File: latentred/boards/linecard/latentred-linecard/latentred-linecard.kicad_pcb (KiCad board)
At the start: 4 copper layers, 220 x 92 mm, 439 parts, among them J1 CONN_LATENTRED_LINECARD_DEVICE, J2 STEWART_SS_74500_024, Q1 SSM6N58NU, Q2 SSM6N58NU, Q3 SSM6N58NU, Q4 SSM6N58NU, Q5 SSM6N58NU, Q6 SSM6N58NU, Q7 SSM6N58NU, Q8 SSM6N58NU, U1 MCP1703T-3302E, U10 DP83867, U11 DP83867, U12 DP83867, U13 DP83867, U14 DP83867, U15 DP83867, U16 DSC6101CI2A-025.0000, U17 5PB1108CMG, U2 LTC3374-QFN, U3 SI7050, U4 LTC2451, U5 INA226, U6 INA226, U7 INA226, U8 DP83867, U9 DP83867

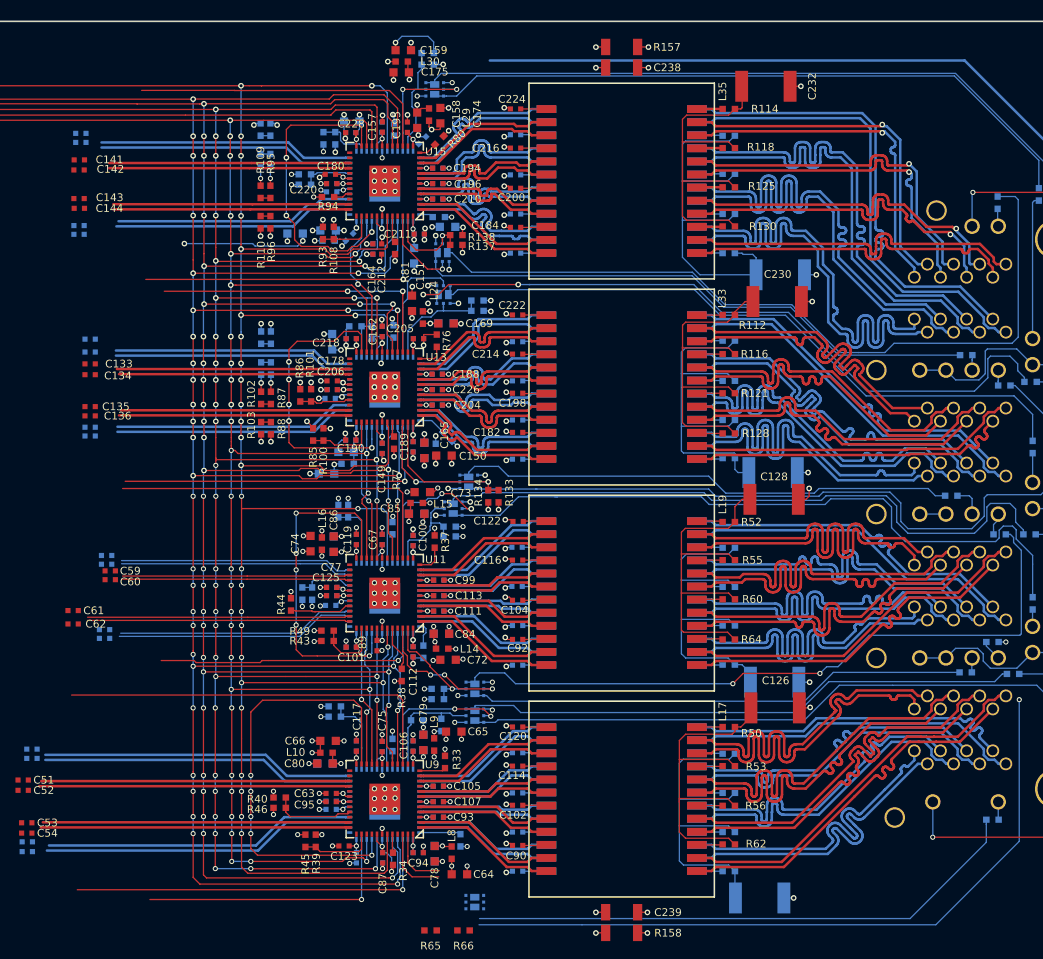
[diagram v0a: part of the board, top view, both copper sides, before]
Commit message: Removed meanders from MDI traces as per Intel layout manual. Now only doing skew matching.
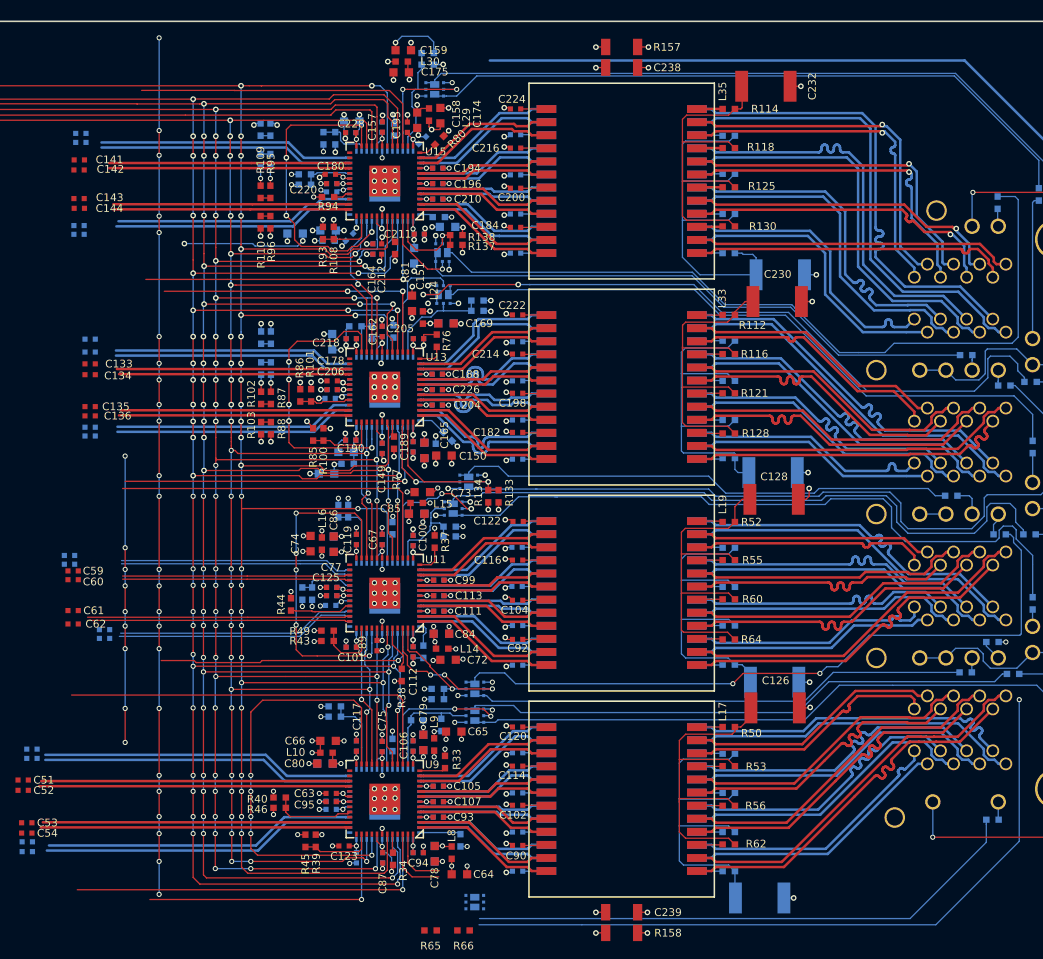
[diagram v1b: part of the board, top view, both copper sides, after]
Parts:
- moved C57 3.60 mm to (170.4, 66.2)
- moved C58 3.60 mm to (170.4, 65.3)
- moved C59 3.60 mm to (170.8, 66.8)
- moved C60 3.60 mm to (170.8, 67.7)
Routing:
- net /PHYs/2V5: track 189.6 -> 255.2 mm, vias 5 -> 29
- net /PHYs/1V0: track 130.2 -> 155.9 mm, vias 8 -> 17
- net /PHYs/ETH6_DM_N: track 46.5 -> 28.8 mm
- net /PHYs/ETH6_DM_P: track 46.5 -> 28.8 mm
- net /PHYs/ETH4_DM_N: track 36.6 -> 23.9 mm
- net /PHYs/ETH4_DM_P: track 36.6 -> 23.9 mm
- net /PHYs/ETH1_DM_N: track 37.1 -> 24.9 mm
- net /PHYs/ETH1_DM_P: track 37.1 -> 24.9 mm
- net /PHYs/ETH6_CM_N: track 46.5 -> 34.5 mm
- net /PHYs/ETH6_CM_P: track 46.5 -> 34.5 mm
- net /PHYs/ETH3_DM_N: track 34.6 -> 23.1 mm
- net /PHYs/ETH3_DM_P: track 34.6 -> 23.1 mm
- net /PHYs/ETH2_DM_P: track 34.1 -> 23.7 mm
- net /PHYs/ETH2_DM_N: track 34.1 -> 23.7 mm
- net /PHYs/ETH4_CM_N: track 36.6 -> 28.4 mm
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
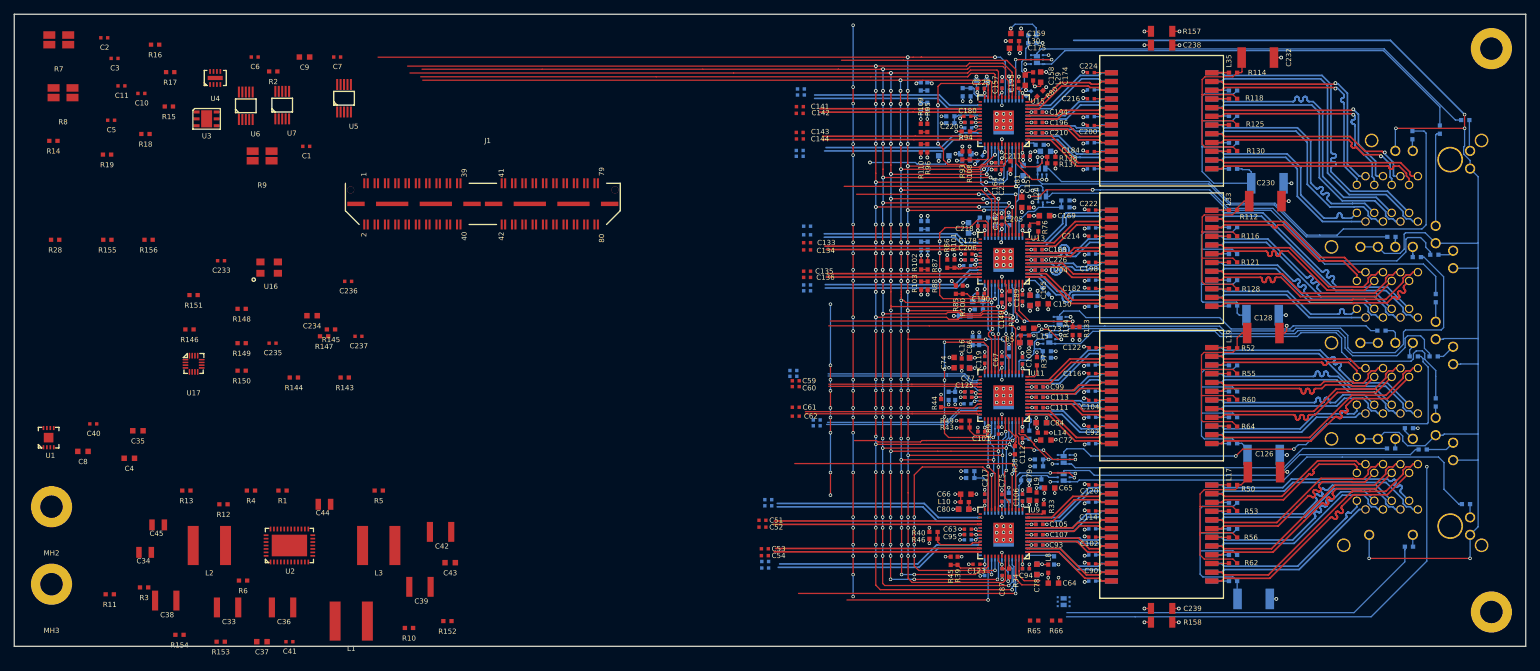
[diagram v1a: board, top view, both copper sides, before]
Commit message: Continued initial line card layout
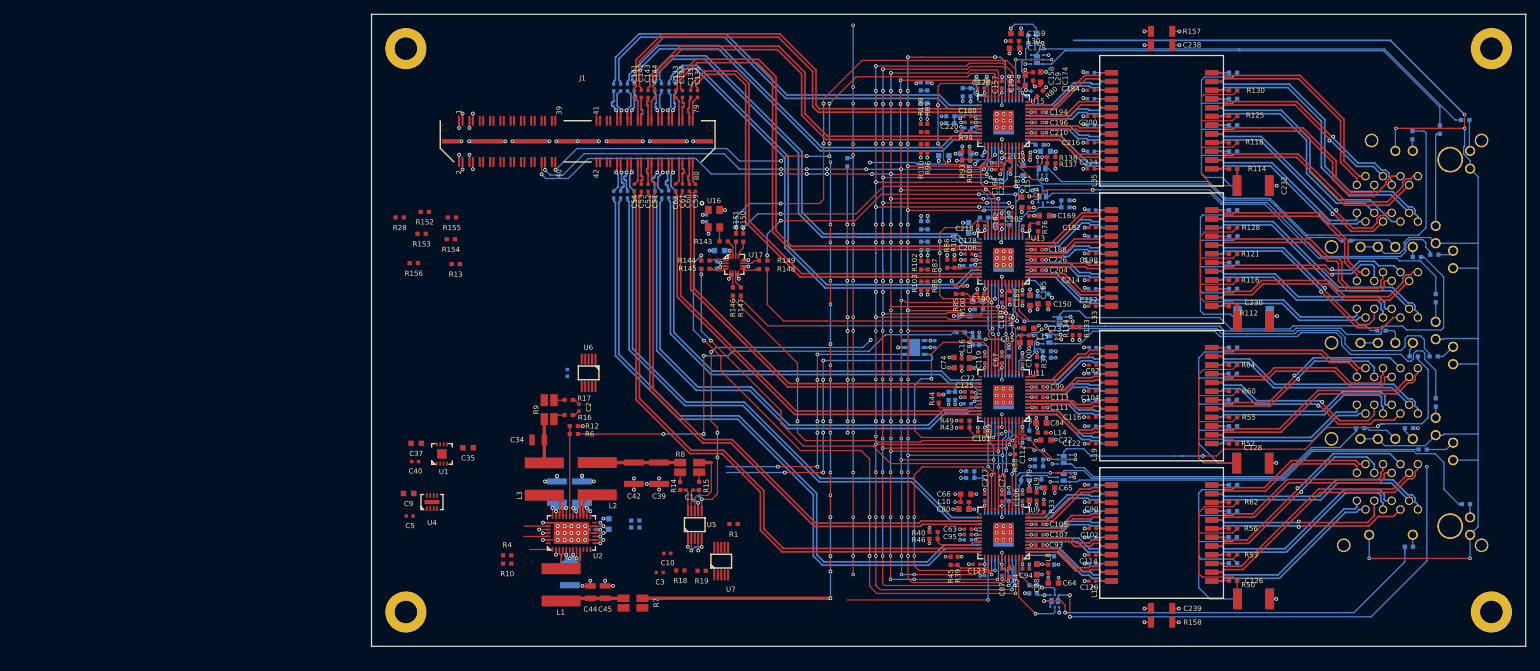
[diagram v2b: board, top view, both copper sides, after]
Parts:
- removed C4, C8: 4.7 uF, azonenberg_pcb:EIA_0603_CAP_NOSILK
- C11, C233, C234, C235, C236, C237, C33, C36, C38, C41, C43, C6, C7, R11, R2, R3, R5, R65, R66, U3: moved to B.Cu
- moved R3 124.5 mm to (194.8, 59.8)
- moved R7 117.1 mm to (147.1, 99.2), turned to 180 degrees
- moved C3 109.1 mm to (150.9, 94.8)
- moved U3 108.3 mm to (188.1, 62.0)
- moved C6 107.5 mm to (191.0, 61.5), turned to 90 degrees
- moved R8 106.3 mm to (155.3, 79.5), turned to 180 degrees
- moved R19 105.6 mm to (157.1, 94.5)
- moved R14 104.1 mm to (153.9, 82.2), turned to 270 degrees
- moved C10 101.7 mm to (152.1, 92.0)
- moved R18 100.5 mm to (153.9, 94.5)
- moved R15 94.9 mm to (156.7, 82.2), turned to 270 degrees
- moved U7 92.1 mm to (159.9, 93.1)
- moved C2 87.6 mm to (139.2, 70.8), turned to 90 degrees
- moved R2 84.6 mm to (178.2, 35.0), turned to 90 degrees
- moved MH2 84.3 mm to (114.0, 18.5), turned to 45 degrees
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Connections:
- J1 pad 18: /JTAG_TDI -> (no net)
- J1 pad 20: /JTAG_TDO -> (no net)
- J1 pad 22: /JTAG_TMS -> (no net)
- J1 pad 24: /JTAG_TCK -> (no net)
- J1 pad 34: (no net) -> /JTAG_TCK
- J1 pad 36: (no net) -> /JTAG_TMS
- J1 pad 38: (no net) -> /JTAG_TDI
- J1 pad 40: /PHYs/SGMII0_TX_P -> /JTAG_TDO
- J1 pad 41: /SGMII0_RX_P -> (no net)
- J1 pad 42: /PHYs/SGMII0_TX_N -> (no net)
- J1 pad 43: /SGMII0_RX_N -> (no net)
- J1 pad 44: /PHYs/SGMII1_TX_P -> (no net)
- J1 pad 45: /SGMII1_RX_P -> (no net)
- J1 pad 46: /PHYs/SGMII1_TX_N -> (no net)
- J1 pad 47: /SGMII1_RX_N -> (no net)
- J1 pad 48: /PHYs/SGMII2_TX_P -> (no net)
- J1 pad 49: /SGMII2_RX_P -> /SGMII6_RX_N
- J1 pad 50: /PHYs/SGMII2_TX_N -> /PHYs/SGMII0_TX_P
- J1 pad 51: /SGMII2_RX_N -> /SGMII6_RX_P
- J1 pad 52: /PHYs/SGMII3_TX_P -> /PHYs/SGMII0_TX_N
- J1 pad 53: /SGMII3_RX_P -> /PHYs/SGMII6_TX_N
- J1 pad 54: /PHYs/SGMII3_TX_N -> /SGMII0_RX_P
- J1 pad 55: /SGMII3_RX_N -> /PHYs/SGMII6_TX_P
- J1 pad 56: /PHYs/SGMII4_TX_P -> /SGMII0_RX_N
- J1 pad 57: /SGMII4_RX_P -> /PHYs/SGMII7_TX_P
- J1 pad 58: /PHYs/SGMII4_TX_N -> /SGMII1_RX_N
- J1 pad 59: /SGMII4_RX_N -> /PHYs/SGMII7_TX_N
- J1 pad 60: /PHYs/SGMII5_TX_P -> /SGMII1_RX_P
- J1 pad 61: /SGMII5_RX_P -> /SGMII7_RX_P
- J1 pad 62: /PHYs/SGMII5_TX_N -> /PHYs/SGMII1_TX_N
- J1 pad 63: /SGMII5_RX_N -> /SGMII7_RX_N
- J1 pad 64: /PHYs/SGMII6_TX_P -> /PHYs/SGMII1_TX_P
- J1 pad 65: /SGMII6_RX_P -> /SGMII4_RX_N
- J1 pad 66: /PHYs/SGMII6_TX_N -> /PHYs/SGMII2_TX_P
- J1 pad 67: /SGMII6_RX_N -> /SGMII4_RX_P
- J1 pad 68: /PHYs/SGMII7_TX_P -> /PHYs/SGMII2_TX_N
- J1 pad 69: /SGMII7_RX_P -> /PHYs/SGMII4_TX_N
- J1 pad 70: /PHYs/SGMII7_TX_N -> /SGMII2_RX_P
- J1 pad 71: /SGMII7_RX_N -> /PHYs/SGMII4_TX_P
- J1 pad 72: (no net) -> /SGMII2_RX_N
- J1 pad 73: (no net) -> /PHYs/SGMII5_TX_P
- J1 pad 74: (no net) -> /SGMII3_RX_N
- J1 pad 75: (no net) -> /PHYs/SGMII5_TX_N
- J1 pad 76: (no net) -> /SGMII3_RX_P
- J1 pad 77: (no net) -> /SGMII5_RX_P
- J1 pad 78: (no net) -> /PHYs/SGMII3_TX_N
- J1 pad 79: (no net) -> /SGMII5_RX_N
- J1 pad 80: (no net) -> /PHYs/SGMII3_TX_P
- J2 pad A4: /PHYs/ETH0_BM_N -> /PHYs/ETH0_CM_P
- J2 pad A5: /PHYs/ETH0_CM_P -> /PHYs/ETH0_CM_N
- J2 pad A6: /PHYs/ETH0_CM_N -> /PHYs/ETH0_BM_N
- J2 pad B4: /PHYs/ETH1_BM_N -> /PHYs/ETH1_CM_P
- J2 pad B5: /PHYs/ETH1_CM_P -> /PHYs/ETH1_CM_N
- J2 pad B6: /PHYs/ETH1_CM_N -> /PHYs/ETH1_BM_N
- J2 pad C4: /PHYs/ETH2_BM_N -> /PHYs/ETH2_CM_P
- J2 pad C5: /PHYs/ETH2_CM_P -> /PHYs/ETH2_CM_N
- J2 pad C6: /PHYs/ETH2_CM_N -> /PHYs/ETH2_BM_N
- J2 pad D4: /PHYs/ETH3_BM_N -> /PHYs/ETH3_CM_P
- J2 pad D5: /PHYs/ETH3_CM_P -> /PHYs/ETH3_CM_N
- J2 pad D6: /PHYs/ETH3_CM_N -> /PHYs/ETH3_BM_N
- J2 pad E4: /PHYs/ETH4_BM_N -> /PHYs/ETH4_CM_P
- J2 pad E5: /PHYs/ETH4_CM_P -> /PHYs/ETH4_CM_N
- J2 pad E6: /PHYs/ETH4_CM_N -> /PHYs/ETH4_BM_N
- J2 pad F4: /PHYs/ETH5_BM_N -> /PHYs/ETH5_CM_P
- J2 pad F5: /PHYs/ETH5_CM_P -> /PHYs/ETH5_CM_N
- J2 pad F6: /PHYs/ETH5_CM_N -> /PHYs/ETH5_BM_N
- J2 pad G4: /PHYs/ETH6_BM_N -> /PHYs/ETH6_CM_P
- J2 pad G5: /PHYs/ETH6_CM_P -> /PHYs/ETH6_CM_N
- J2 pad G6: /PHYs/ETH6_CM_N -> /PHYs/ETH6_BM_N
- J2 pad H4: /PHYs/ETH7_BM_N -> /PHYs/ETH7_CM_P
- J2 pad H5: /PHYs/ETH7_CM_P -> /PHYs/ETH7_CM_N
- J2 pad H6: /PHYs/ETH7_CM_N -> /PHYs/ETH7_BM_N
- L17 pad 1: Net-(C120-Pad2) -> Net-(L17-Pad1)
- L17 pad 10: Net-(C90-Pad2) -> Net-(L17-Pad10)
- L17 pad 11: /PHYs/ETH1_A_N -> /PHYs/ETH1_DM_N
- L17 pad 12: /PHYs/ETH1_A_P -> /PHYs/ETH1_DM_P
- L17 pad 13: /PHYs/ETH1_AM_N -> /PHYs/ETH1_D_N
- L17 pad 14: /PHYs/ETH1_AM_P -> /PHYs/ETH1_D_P
- L17 pad 15: Net-(L17-Pad15) -> Net-(C90-Pad2)
- L17 pad 16: /PHYs/ETH1_BM_N -> /PHYs/ETH1_C_N
- L17 pad 17: /PHYs/ETH1_BM_P -> /PHYs/ETH1_C_P
- L17 pad 18: Net-(L17-Pad18) -> Net-(C102-Pad2)
- L17 pad 19: /PHYs/ETH1_CM_N -> /PHYs/ETH1_B_N
- L17 pad 2: /PHYs/ETH1_D_N -> /PHYs/ETH1_AM_P
- L17 pad 20: /PHYs/ETH1_CM_P -> /PHYs/ETH1_B_P
- L17 pad 21: Net-(L17-Pad21) -> Net-(C114-Pad2)
- L17 pad 22: /PHYs/ETH1_DM_N -> /PHYs/ETH1_A_N
- L17 pad 23: /PHYs/ETH1_DM_P -> /PHYs/ETH1_A_P
- L17 pad 24: Net-(L17-Pad24) -> Net-(C120-Pad2)
- L17 pad 3: /PHYs/ETH1_D_P -> /PHYs/ETH1_AM_N
- L17 pad 4: Net-(C114-Pad2) -> Net-(L17-Pad4)
- L17 pad 5: /PHYs/ETH1_C_N -> /PHYs/ETH1_BM_N
- L17 pad 6: /PHYs/ETH1_C_P -> /PHYs/ETH1_BM_P
- L17 pad 7: Net-(C102-Pad2) -> Net-(L17-Pad7)
- L17 pad 8: /PHYs/ETH1_B_N -> /PHYs/ETH1_CM_P
- L17 pad 9: /PHYs/ETH1_B_P -> /PHYs/ETH1_CM_N
- L18 pad 1: Net-(C121-Pad2) -> Net-(L18-Pad1)
- L18 pad 10: Net-(C91-Pad2) -> Net-(L18-Pad10)
- L18 pad 11: /PHYs/ETH2_A_N -> /PHYs/ETH2_DM_N
- L18 pad 12: /PHYs/ETH2_A_P -> /PHYs/ETH2_DM_P
- L18 pad 13: /PHYs/ETH2_AM_N -> /PHYs/ETH2_D_N
- L18 pad 14: /PHYs/ETH2_AM_P -> /PHYs/ETH2_D_P
- L18 pad 15: Net-(L18-Pad15) -> Net-(C91-Pad2)
- L18 pad 16: /PHYs/ETH2_BM_N -> /PHYs/ETH2_C_N
- L18 pad 17: /PHYs/ETH2_BM_P -> /PHYs/ETH2_C_P
- L18 pad 18: Net-(L18-Pad18) -> Net-(C103-Pad2)
- L18 pad 19: /PHYs/ETH2_CM_N -> /PHYs/ETH2_B_N
- L18 pad 2: /PHYs/ETH2_D_N -> /PHYs/ETH2_AM_P
- L18 pad 20: /PHYs/ETH2_CM_P -> /PHYs/ETH2_B_P
- L18 pad 21: Net-(L18-Pad21) -> Net-(C115-Pad2)
- L18 pad 22: /PHYs/ETH2_DM_N -> /PHYs/ETH2_A_N
- L18 pad 23: /PHYs/ETH2_DM_P -> /PHYs/ETH2_A_P
- L18 pad 24: Net-(L18-Pad24) -> Net-(C121-Pad2)
- L18 pad 3: /PHYs/ETH2_D_P -> /PHYs/ETH2_AM_N
- L18 pad 4: Net-(C115-Pad2) -> Net-(L18-Pad4)
- L18 pad 5: /PHYs/ETH2_C_N -> /PHYs/ETH2_BM_N
- L18 pad 6: /PHYs/ETH2_C_P -> /PHYs/ETH2_BM_P
- L18 pad 7: Net-(C103-Pad2) -> Net-(L18-Pad7)
- L18 pad 8: /PHYs/ETH2_B_N -> /PHYs/ETH2_CM_P
- L18 pad 9: /PHYs/ETH2_B_P -> /PHYs/ETH2_CM_N
- L19 pad 1: Net-(C122-Pad2) -> Net-(L19-Pad1)
- L19 pad 10: Net-(C92-Pad2) -> Net-(L19-Pad10)
- L19 pad 11: /PHYs/ETH3_A_N -> /PHYs/ETH3_DM_N
- L19 pad 12: /PHYs/ETH3_A_P -> /PHYs/ETH3_DM_P
- L19 pad 13: /PHYs/ETH3_AM_N -> /PHYs/ETH3_D_N
- L19 pad 14: /PHYs/ETH3_AM_P -> /PHYs/ETH3_D_P
- L19 pad 15: Net-(L19-Pad15) -> Net-(C92-Pad2)
- L19 pad 16: /PHYs/ETH3_BM_N -> /PHYs/ETH3_C_N
- L19 pad 17: /PHYs/ETH3_BM_P -> /PHYs/ETH3_C_P
- L19 pad 18: Net-(L19-Pad18) -> Net-(C104-Pad2)
- L19 pad 19: /PHYs/ETH3_CM_N -> /PHYs/ETH3_B_N
- L19 pad 2: /PHYs/ETH3_D_N -> /PHYs/ETH3_AM_P
- L19 pad 20: /PHYs/ETH3_CM_P -> /PHYs/ETH3_B_P
- L19 pad 21: Net-(L19-Pad21) -> Net-(C116-Pad2)
- L19 pad 22: /PHYs/ETH3_DM_N -> /PHYs/ETH3_A_N
- L19 pad 23: /PHYs/ETH3_DM_P -> /PHYs/ETH3_A_P
- L19 pad 24: Net-(L19-Pad24) -> Net-(C122-Pad2)
- L19 pad 3: /PHYs/ETH3_D_P -> /PHYs/ETH3_AM_N
- L19 pad 4: Net-(C116-Pad2) -> Net-(L19-Pad4)
- L19 pad 5: /PHYs/ETH3_C_N -> /PHYs/ETH3_BM_N
- L19 pad 6: /PHYs/ETH3_C_P -> /PHYs/ETH3_BM_P
- L19 pad 7: Net-(C104-Pad2) -> Net-(L19-Pad7)
- L19 pad 8: /PHYs/ETH3_B_N -> /PHYs/ETH3_CM_P
- L19 pad 9: /PHYs/ETH3_B_P -> /PHYs/ETH3_CM_N
- L32 pad 1: Net-(C221-Pad2) -> Net-(L32-Pad1)
- L32 pad 10: Net-(C181-Pad2) -> Net-(L32-Pad10)
- L32 pad 11: /PHYs/ETH4_A_N -> /PHYs/ETH4_DM_N
- L32 pad 12: /PHYs/ETH4_A_P -> /PHYs/ETH4_DM_P
- L32 pad 13: /PHYs/ETH4_AM_N -> /PHYs/ETH4_D_N
- L32 pad 14: /PHYs/ETH4_AM_P -> /PHYs/ETH4_D_P
- L32 pad 15: Net-(L32-Pad15) -> Net-(C181-Pad2)
- L32 pad 16: /PHYs/ETH4_BM_N -> /PHYs/ETH4_C_N
- L32 pad 17: /PHYs/ETH4_BM_P -> /PHYs/ETH4_C_P
- L32 pad 18: Net-(L32-Pad18) -> Net-(C197-Pad2)
- L32 pad 19: /PHYs/ETH4_CM_N -> /PHYs/ETH4_B_N
- L32 pad 2: /PHYs/ETH4_D_N -> /PHYs/ETH4_AM_P
- L32 pad 20: /PHYs/ETH4_CM_P -> /PHYs/ETH4_B_P
- L32 pad 21: Net-(L32-Pad21) -> Net-(C213-Pad2)
- L32 pad 22: /PHYs/ETH4_DM_N -> /PHYs/ETH4_A_N
- L32 pad 23: /PHYs/ETH4_DM_P -> /PHYs/ETH4_A_P
- L32 pad 24: Net-(L32-Pad24) -> Net-(C221-Pad2)
- L32 pad 3: /PHYs/ETH4_D_P -> /PHYs/ETH4_AM_N
- L32 pad 4: Net-(C213-Pad2) -> Net-(L32-Pad4)
- L32 pad 5: /PHYs/ETH4_C_N -> /PHYs/ETH4_BM_N
- L32 pad 6: /PHYs/ETH4_C_P -> /PHYs/ETH4_BM_P
- L32 pad 7: Net-(C197-Pad2) -> Net-(L32-Pad7)
- L32 pad 8: /PHYs/ETH4_B_N -> /PHYs/ETH4_CM_P
- L32 pad 9: /PHYs/ETH4_B_P -> /PHYs/ETH4_CM_N
- L33 pad 1: Net-(C222-Pad2) -> Net-(L33-Pad1)
- L33 pad 10: Net-(C182-Pad2) -> Net-(L33-Pad10)
- L33 pad 11: /PHYs/ETH5_A_N -> /PHYs/ETH5_DM_N
- L33 pad 12: /PHYs/ETH5_A_P -> /PHYs/ETH5_DM_P
- L33 pad 13: /PHYs/ETH5_AM_N -> /PHYs/ETH5_D_N
- L33 pad 14: /PHYs/ETH5_AM_P -> /PHYs/ETH5_D_P
- L33 pad 15: Net-(L33-Pad15) -> Net-(C182-Pad2)
- L33 pad 16: /PHYs/ETH5_BM_N -> /PHYs/ETH5_C_N
- L33 pad 17: /PHYs/ETH5_BM_P -> /PHYs/ETH5_C_P
- L33 pad 18: Net-(L33-Pad18) -> Net-(C198-Pad2)
- L33 pad 19: /PHYs/ETH5_CM_N -> /PHYs/ETH5_B_N
- L33 pad 2: /PHYs/ETH5_D_N -> /PHYs/ETH5_AM_N
- L33 pad 20: /PHYs/ETH5_CM_P -> /PHYs/ETH5_B_P
- L33 pad 21: Net-(L33-Pad21) -> Net-(C214-Pad2)
- L33 pad 22: /PHYs/ETH5_DM_N -> /PHYs/ETH5_A_N
- L33 pad 23: /PHYs/ETH5_DM_P -> /PHYs/ETH5_A_P
- L33 pad 24: Net-(L33-Pad24) -> Net-(C222-Pad2)
- L33 pad 3: /PHYs/ETH5_D_P -> /PHYs/ETH5_AM_P
- L33 pad 4: Net-(C214-Pad2) -> Net-(L33-Pad4)
- L33 pad 5: /PHYs/ETH5_C_N -> /PHYs/ETH5_BM_N
- L33 pad 6: /PHYs/ETH5_C_P -> /PHYs/ETH5_BM_P
- L33 pad 7: Net-(C198-Pad2) -> Net-(L33-Pad7)
- L33 pad 8: /PHYs/ETH5_B_N -> /PHYs/ETH5_CM_P
- L33 pad 9: /PHYs/ETH5_B_P -> /PHYs/ETH5_CM_N
- L34 pad 1: Net-(C223-Pad2) -> Net-(L34-Pad1)
- L34 pad 10: Net-(C183-Pad2) -> Net-(L34-Pad10)
- L34 pad 11: /PHYs/ETH6_A_N -> /PHYs/ETH6_DM_N
- L34 pad 12: /PHYs/ETH6_A_P -> /PHYs/ETH6_DM_P
- L34 pad 13: /PHYs/ETH6_AM_N -> /PHYs/ETH6_D_N
- L34 pad 14: /PHYs/ETH6_AM_P -> /PHYs/ETH6_D_P
- L34 pad 15: Net-(L34-Pad15) -> Net-(C183-Pad2)
- L34 pad 16: /PHYs/ETH6_BM_N -> /PHYs/ETH6_C_N
- L34 pad 17: /PHYs/ETH6_BM_P -> /PHYs/ETH6_C_P
- L34 pad 18: Net-(L34-Pad18) -> Net-(C199-Pad2)
- L34 pad 19: /PHYs/ETH6_CM_N -> /PHYs/ETH6_B_N
- L34 pad 2: /PHYs/ETH6_D_N -> /PHYs/ETH6_AM_P
- L34 pad 20: /PHYs/ETH6_CM_P -> /PHYs/ETH6_B_P
- L34 pad 21: Net-(L34-Pad21) -> Net-(C215-Pad2)
- L34 pad 22: /PHYs/ETH6_DM_N -> /PHYs/ETH6_A_N
- L34 pad 23: /PHYs/ETH6_DM_P -> /PHYs/ETH6_A_P
- L34 pad 24: Net-(L34-Pad24) -> Net-(C223-Pad2)
- L34 pad 3: /PHYs/ETH6_D_P -> /PHYs/ETH6_AM_N
- L34 pad 4: Net-(C215-Pad2) -> Net-(L34-Pad4)
- L34 pad 5: /PHYs/ETH6_C_N -> /PHYs/ETH6_BM_P
- L34 pad 6: /PHYs/ETH6_C_P -> /PHYs/ETH6_BM_N
- L34 pad 7: Net-(C199-Pad2) -> Net-(L34-Pad7)
- L34 pad 8: /PHYs/ETH6_B_N -> /PHYs/ETH6_CM_P
- L34 pad 9: /PHYs/ETH6_B_P -> /PHYs/ETH6_CM_N
- L35 pad 1: Net-(C224-Pad2) -> Net-(L35-Pad1)
- L35 pad 10: Net-(C184-Pad2) -> Net-(L35-Pad10)
- L35 pad 11: /PHYs/ETH7_A_N -> /PHYs/ETH7_DM_N
- L35 pad 12: /PHYs/ETH7_A_P -> /PHYs/ETH7_DM_P
- L35 pad 13: /PHYs/ETH7_AM_N -> /PHYs/ETH7_D_N
- L35 pad 14: /PHYs/ETH7_AM_P -> /PHYs/ETH7_D_P
- L35 pad 15: Net-(L35-Pad15) -> Net-(C184-Pad2)
- L35 pad 16: /PHYs/ETH7_BM_N -> /PHYs/ETH7_C_N
- L35 pad 17: /PHYs/ETH7_BM_P -> /PHYs/ETH7_C_P
- L35 pad 18: Net-(L35-Pad18) -> Net-(C200-Pad2)
- L35 pad 19: /PHYs/ETH7_CM_N -> /PHYs/ETH7_B_N
- L35 pad 2: /PHYs/ETH7_D_N -> /PHYs/ETH7_AM_N
- L35 pad 20: /PHYs/ETH7_CM_P -> /PHYs/ETH7_B_P
- L35 pad 21: Net-(L35-Pad21) -> Net-(C216-Pad2)
- L35 pad 22: /PHYs/ETH7_DM_N -> /PHYs/ETH7_A_N
- L35 pad 23: /PHYs/ETH7_DM_P -> /PHYs/ETH7_A_P
- L35 pad 24: Net-(L35-Pad24) -> Net-(C224-Pad2)
- L35 pad 3: /PHYs/ETH7_D_P -> /PHYs/ETH7_AM_P
- L35 pad 4: Net-(C216-Pad2) -> Net-(L35-Pad4)
- L35 pad 5: /PHYs/ETH7_C_N -> /PHYs/ETH7_BM_P
- L35 pad 6: /PHYs/ETH7_C_P -> /PHYs/ETH7_BM_N
- L35 pad 7: Net-(C200-Pad2) -> Net-(L35-Pad7)
- L35 pad 8: /PHYs/ETH7_B_N -> /PHYs/ETH7_CM_N
- L35 pad 9: /PHYs/ETH7_B_P -> /PHYs/ETH7_CM_P
- L7 pad 1: Net-(C49-Pad2) -> Net-(L7-Pad1)
- L7 pad 10: Net-(C46-Pad2) -> Net-(L7-Pad10)
- L7 pad 11: /PHYs/ETH0_A_N -> /PHYs/ETH0_DM_N
- L7 pad 12: /PHYs/ETH0_A_P -> /PHYs/ETH0_DM_P
- L7 pad 13: /PHYs/ETH0_AM_N -> /PHYs/ETH0_D_N
- L7 pad 14: /PHYs/ETH0_AM_P -> /PHYs/ETH0_D_P
- L7 pad 15: Net-(L7-Pad15) -> Net-(C46-Pad2)
- L7 pad 16: /PHYs/ETH0_BM_N -> /PHYs/ETH0_C_N
- L7 pad 17: /PHYs/ETH0_BM_P -> /PHYs/ETH0_C_P
- L7 pad 18: Net-(L7-Pad18) -> Net-(C47-Pad2)
- L7 pad 19: /PHYs/ETH0_CM_N -> /PHYs/ETH0_B_N
- L7 pad 2: /PHYs/ETH0_D_N -> /PHYs/ETH0_AM_P
- L7 pad 20: /PHYs/ETH0_CM_P -> /PHYs/ETH0_B_P
- L7 pad 21: Net-(L7-Pad21) -> Net-(C48-Pad2)
- L7 pad 22: /PHYs/ETH0_DM_N -> /PHYs/ETH0_A_N
- L7 pad 23: /PHYs/ETH0_DM_P -> /PHYs/ETH0_A_P
- L7 pad 24: Net-(L7-Pad24) -> Net-(C49-Pad2)
- L7 pad 3: /PHYs/ETH0_D_P -> /PHYs/ETH0_AM_N
- L7 pad 4: Net-(C48-Pad2) -> Net-(L7-Pad4)
- L7 pad 5: /PHYs/ETH0_C_N -> /PHYs/ETH0_BM_N
- L7 pad 6: /PHYs/ETH0_C_P -> /PHYs/ETH0_BM_P
- L7 pad 7: Net-(C47-Pad2) -> Net-(L7-Pad7)
- L7 pad 8: /PHYs/ETH0_B_N -> /PHYs/ETH0_CM_P
- L7 pad 9: /PHYs/ETH0_B_P -> /PHYs/ETH0_CM_N
- R111 pad 2: Net-(L32-Pad24) -> Net-(L32-Pad1)
- R112 pad 2: Net-(L33-Pad24) -> Net-(L33-Pad1)
- R113 pad 2: Net-(L34-Pad24) -> Net-(L34-Pad1)
- R114 pad 2: Net-(L35-Pad24) -> Net-(L35-Pad1)
- R115 pad 2: Net-(L32-Pad21) -> Net-(L32-Pad4)
- R116 pad 2: Net-(L33-Pad21) -> Net-(L33-Pad4)
- R117 pad 2: Net-(L34-Pad21) -> Net-(L34-Pad4)
- R118 pad 2: Net-(L35-Pad21) -> Net-(L35-Pad4)
- R119 pad 2: Net-(L32-Pad18) -> Net-(L32-Pad7)
- R121 pad 2: Net-(L33-Pad18) -> Net-(L33-Pad7)
- R123 pad 2: Net-(L34-Pad18) -> Net-(L34-Pad7)
- R125 pad 2: Net-(L35-Pad18) -> Net-(L35-Pad7)
- R127 pad 2: Net-(L32-Pad15) -> Net-(L32-Pad10)
- R128 pad 2: Net-(L33-Pad15) -> Net-(L33-Pad10)
- R129 pad 2: Net-(L34-Pad15) -> Net-(L34-Pad10)
- R130 pad 2: Net-(L35-Pad15) -> Net-(L35-Pad10)
- R29 pad 2: Net-(L7-Pad24) -> Net-(L7-Pad1)
- R30 pad 2: Net-(L7-Pad21) -> Net-(L7-Pad4)
- R31 pad 2: Net-(L7-Pad18) -> Net-(L7-Pad7)
- R32 pad 2: Net-(L7-Pad15) -> Net-(L7-Pad10)
- R50 pad 2: Net-(L17-Pad24) -> Net-(L17-Pad1)
- R51 pad 2: Net-(L18-Pad24) -> Net-(L18-Pad1)
- R52 pad 2: Net-(L19-Pad24) -> Net-(L19-Pad1)
- R53 pad 2: Net-(L17-Pad21) -> Net-(L17-Pad4)
- R54 pad 2: Net-(L18-Pad21) -> Net-(L18-Pad4)
- R55 pad 2: Net-(L19-Pad21) -> Net-(L19-Pad4)
- R56 pad 2: Net-(L17-Pad18) -> Net-(L17-Pad7)
- R58 pad 2: Net-(L18-Pad18) -> Net-(L18-Pad7)
- R60 pad 2: Net-(L19-Pad18) -> Net-(L19-Pad7)
- R62 pad 2: Net-(L17-Pad15) -> Net-(L17-Pad10)
- R63 pad 2: Net-(L18-Pad15) -> Net-(L18-Pad10)
- R64 pad 2: Net-(L19-Pad15) -> Net-(L19-Pad10)
- U2 pad 10: /Power Supply/2V5_SW -> Net-(U2-Pad10)
- U2 pad 11: /5V0 -> Net-(U2-Pad11)
- U2 pad 12: Net-(R11-Pad2) -> Net-(U2-Pad12)
- U2 pad 13: /2V5_EN -> /GND
- U2 pad 19: /GND -> /2V5_EN
- U2 pad 20: /5V0 -> Net-(R11-Pad2)
- U5 pad 8: /PHYs/1V8 -> /PHYs/2V5
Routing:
- net /GND: track 694.9 -> 1080.0 mm, vias 193 -> 258
- net /PHY_RST_N: track 292.9 -> 216.3 mm, vias 30 -> 24
- net /5V0: track 0.00 -> 70.5 mm, vias 0 -> 20
- net /MGMT_MDC: track 306.7 -> 238.6 mm, vias 33 -> 27
- net /Power Supply/1V8_SENSE: track 0.00 -> 68.0 mm, vias 0 -> 3
- net /MGMT_MDIO: track 295.7 -> 228.6 mm, vias 33 -> 27
- net /PHYs/SGMII0_TX_C_P: track 30.5 -> 95.0 mm
- net /PHYs/SGMII0_TX_C_N: track 30.3 -> 94.2 mm
- net /PHYs/SGMII1_RX_C_N: track 30.0 -> 93.0 mm
- net /PHYs/SGMII1_RX_C_P: track 29.8 -> 92.2 mm
- net /3V3: track 0.00 -> 60.6 mm, vias 0 -> 6
- net /PHYs/1V8: track 450.5 -> 509.3 mm, vias 57 -> 64
- net /PHYs/SGMII1_TX_C_N: track 30.2 -> 85.5 mm
- net /PHYs/CLK_25MHZ_0: track 36.5 -> 91.8 mm, vias 1 -> 5
- net /PHYs/SGMII1_TX_C_P: track 29.9 -> 84.7 mm
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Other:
- board size 220 x 92 mm -> 168 x 92 mm

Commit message: Updating file: latentred-linecard.kicad_pcb with current fully routed design
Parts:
- added R159: 1K, azonenberg_pcb:EIA_0402_RES_NOSILK, F.Cu at (136.3, 38.4)
- C3, C35, C40, C5, R1, R18, R19, U7: moved to B.Cu
- R11, R5: moved to F.Cu
- moved R1 50.0 mm to (177.0, 40.1), turned to 180 degrees
- moved R13 46.1 mm to (144.8, 89.5), turned to 180 degrees
- moved R155 27.0 mm to (141.1, 60.7), turned to 270 degrees
- moved R156 26.8 mm to (139.6, 60.7), turned to 270 degrees
- moved R28 22.0 mm to (134.8, 39.8), turned to 180 degrees
- moved C40 17.9 mm to (131.9, 71.7), turned to 90 degrees
- moved C37 14.5 mm to (129.9, 74.6), turned to 180 degrees
- moved C5 13.8 mm to (125.5, 94.8), turned to 180 degrees
- moved C9 13.4 mm to (122.5, 93.9), turned to 90 degrees
- moved U7 12.0 mm to (147.9, 93.9)
- moved R152 12.0 mm to (125.6, 50.3), turned to 270 degrees
- moved R153 12.0 mm to (127.4, 41.0), turned to 90 degrees
- moved U4 11.9 mm to (125.3, 93.8)
- moved U1 11.5 mm to (129.2, 71.8), turned to 90 degrees
- moved R19 9.94 mm to (148.4, 99.4), turned to 90 degrees
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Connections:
- J1 pad 11: /MGMT_MDC -> (no net)
- J1 pad 13: /I2C_SDA -> (no net)
- J1 pad 14: /1V8_EN -> /2V5_EN
- J1 pad 15: /I2C_SCL -> (no net)
- J1 pad 16: /2V5_EN -> /1V8_EN
- J1 pad 17: /PHY_RST_N -> (no net)
- J1 pad 30: (no net) -> /I2C_SCL
- J1 pad 32: (no net) -> /I2C_SDA
- J1 pad 33: (no net) -> /JTAG_TDI
- J1 pad 34: /JTAG_TCK -> /MGMT_MDC
- J1 pad 35: (no net) -> /JTAG_TCK
- J1 pad 36: /JTAG_TMS -> /MGMT_MDIO
- J1 pad 37: (no net) -> /JTAG_TMS
- J1 pad 38: /JTAG_TDI -> (no net)
- J1 pad 39: (no net) -> /JTAG_TDO
- J1 pad 40: /JTAG_TDO -> /PHY_RST_N
- J1 pad 9: /MGMT_MDIO -> (no net)
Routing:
- net /JTAG_TDI: track 26.4 -> 176.5 mm, vias 1 -> 3
- net /I2C_SDA: track 44.1 -> 172.3 mm, vias 7 -> 9
- net /I2C_SCL: track 52.8 -> 172.1 mm, vias 8 -> 9
- net /Power Supply/1V0_SENSE: track 0.00 -> 118.1 mm, vias 0 -> 7
- net /GND: track 1080.0 -> 1192.7 mm, vias 258 -> 281
- net /3V3: track 60.6 -> 166.1 mm, vias 6 -> 16
- net /PHYs/3V3: track 225.5 -> 147.7 mm, vias 5 -> 0
- net /PSU_PGOOD: track 0.80 -> 74.6 mm, vias 1 -> 2
- net /PHYs/1V0: track 177.4 -> 248.3 mm, vias 24 -> 75
- net /2V5_EN: track 0.00 -> 69.6 mm, vias 0 -> 2
- net /5V0: track 70.5 -> 139.9 mm, vias 20 -> 21
- net /1V0_EN: track 0.00 -> 65.5 mm
- net /PHY_RST_N: track 216.3 -> 277.0 mm, vias 24 -> 28
- net /1V8_EN: track 3.50 -> 60.5 mm
- net /MGMT_MDIO: track 228.6 -> 285.2 mm, vias 27 -> 30
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- added copper zone on In2.Cu, net /3V3
- added copper zone on In2.Cu, net /5V0
- added copper zone on In1.Cu, net /GND
- added copper zone on B.Cu, net /PHYs/1V0
- added copper zone on F.Cu, net /PHYs/1V0
- added copper zone on In2.Cu, net /PHYs/1V0
- added copper zone on B.Cu, net /PHYs/2V5
- added copper zone on F.Cu, net /PHYs/2V5
- added copper zone on In2.Cu, net /PHYs/2V5
- added copper zone on In2.Cu, net /PHYs/A1V0_1
- added copper zone on In2.Cu, net /PHYs/A1V0_3
- added copper zone on In2.Cu, net /PHYs/A1V0_5
- added copper zone on In2.Cu, net /PHYs/A1V8_3
- added copper zone on In2.Cu, net /PHYs/A1V8_5
- added copper zone on In2.Cu, net /PHYs/A2V5_3
- added copper zone on In2.Cu, net /PHYs/A2V5_5
